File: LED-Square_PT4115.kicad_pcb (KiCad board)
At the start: 2 copper layers, 50 x 50 mm, 28 parts, among them P1 IN, P2 OUT, U1 PT4115-SOT89-5

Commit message: Fooling around a bit.
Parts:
- C1: footprint -C1206 -> my_parts:MADW__C0805
- C2, C3, C4, C5, C6: footprint -C0805 -> my_parts:MADW__C0805
- D1, D2, D3, D4, D5, D6: footprint MADW__Nichia-NSS-LED__handsolder -> my_parts:MADW__Nichia-NT2x757DT
- DS1: value MBRS140T3G -> SS14L (40V, 1A); footprint MADW__diode-SMB-package -> my_parts:MADW__diode_sub-SMA
- DZ1: footprint -SOT23 -> my_parts:MADW__SOT23
- R1, R2, R_CS1: footprint -R0805 -> my_parts:MADW__R0805
- moved DS1 1.60 mm to (82.8, 111.4)
- moved R2 1.05 mm to (92.9, 120.0)
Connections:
- P1 pad 5: (no net) -> Net-(P1-Pad5)
- P2 pad 2: (no net) -> Net-(P2-Pad2)
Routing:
- net GND: track 82.5 -> 192.2 mm, vias 8 -> 19
- net VCC: track 134.0 -> 137.6 mm
- net /SW: track 17.6 -> 14.8 mm
- net /D6HS: track 12.5 -> 11.4 mm
- net /D4HS: track 26.7 -> 27.8 mm
- net /D1HS: track 26.7 -> 27.8 mm
- net /CSN: track 30.9 -> 30.0 mm
- net /_dim: track 20.7 -> 21.3 mm
- removed copper zone on F.Cu, net (none)
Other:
- board text added: "2014 - blog.spitzenpfeil.org"
- board text added: "L1: 100µH RCS_1: 0R6 -> 0.167A D1...: Nichia NT2x757DT equiv."
- board text added: "LED Square V1.1.a"
- board text added: "U1: PT4115 DS1: SS14L DZ1: BZX84C_5V1 R2: 1k"
- board text removed: "2013 - blog.spitzenpfeil.org"
- board text removed: "L1: 100µH RCS_1: 1R -> 0.1A D1...: Nichia NSSL157AT-H3 equiv."
- board text removed: "LED Square V1.0"
- board text removed: "U1: PT4115 DS1: MBRS140T3G DZ1: BZX84C_5V1 R2: 1k"

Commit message: R_CS --> 1206. Couldn't get 1R1 in 0805.
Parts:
- added R_CS2: 1R1, my_parts:MADW__R1206, F.Cu at (77.0, 111.4)
- G1: value LOGO -> OSHW-logo_silkscreen_5mm; footprint (none) -> oshw-logo:OSHW-logo_silkscreen_5mm
- G2: value LOGO -> LED_smile_silkscreen_5mm; footprint LOGO -> led-smile:LED_smile_silkscreen_5mm
- G3: renamed from G6; value LOGO -> KiCad LOGO
- R_CS1: value 1R -> 1R1; footprint my_parts:MADW__R0805 -> my_parts:MADW__R1206
- moved G2 5.00 mm to (87.0, 132.0)
- moved R_CS1 1.01 mm to (74.0, 111.4)
- moved G1 0.26 mm to (87.0, 101.0)
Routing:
- net GND: track 192.2 -> 178.7 mm, vias 19 -> 17
- net VCC: track 137.6 -> 147.0 mm
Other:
- board text added: "L1: 100µH RCS_1: (1R1)/2 -> 0.180A D1...: Nichia NT2x757DT equiv."
- board text added: "LED Square V1.11.a"
- board text removed: "L1: 100µH RCS_1: 0R6 -> 0.167A D1...: Nichia NT2x757DT equiv."
- board text removed: "LED Square V1.1.a"

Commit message: Tweaks.
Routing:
- net GND: track 178.7 -> 173.3 mm

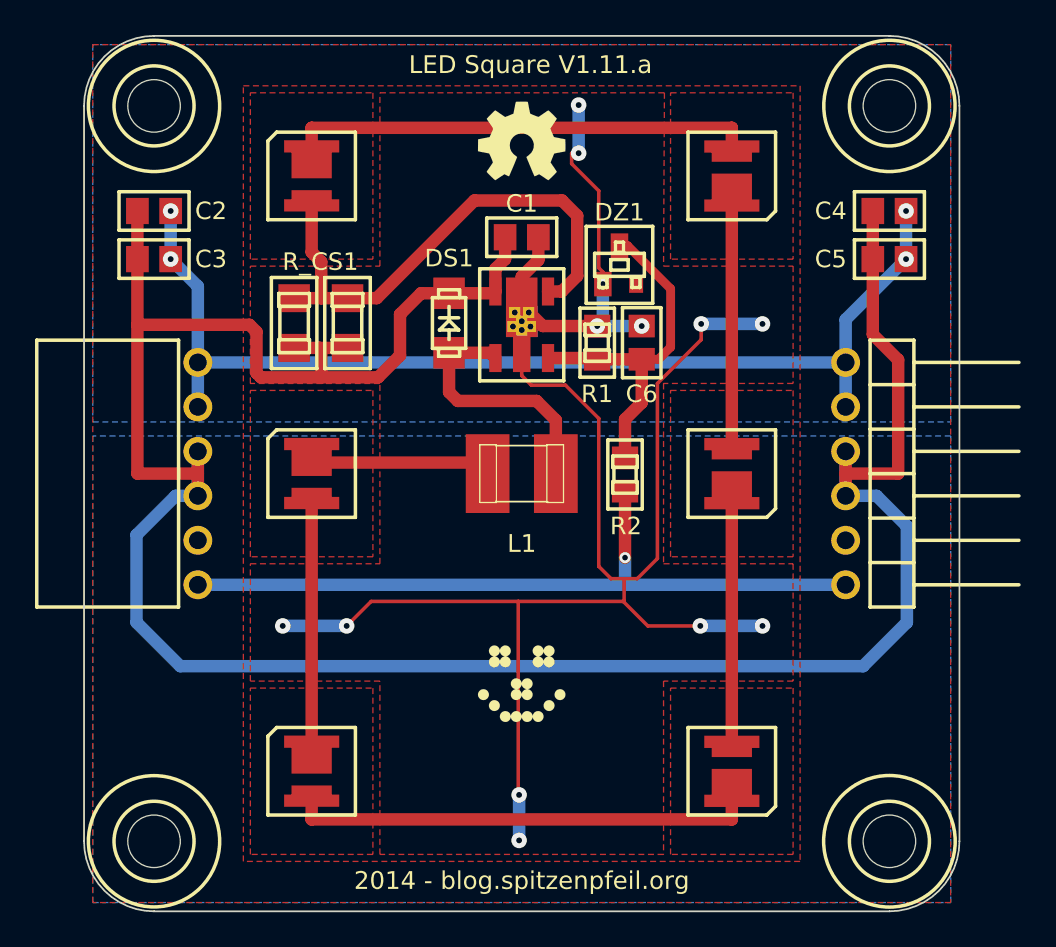
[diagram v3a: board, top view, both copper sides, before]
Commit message: Used B_Cu as heatsink again.
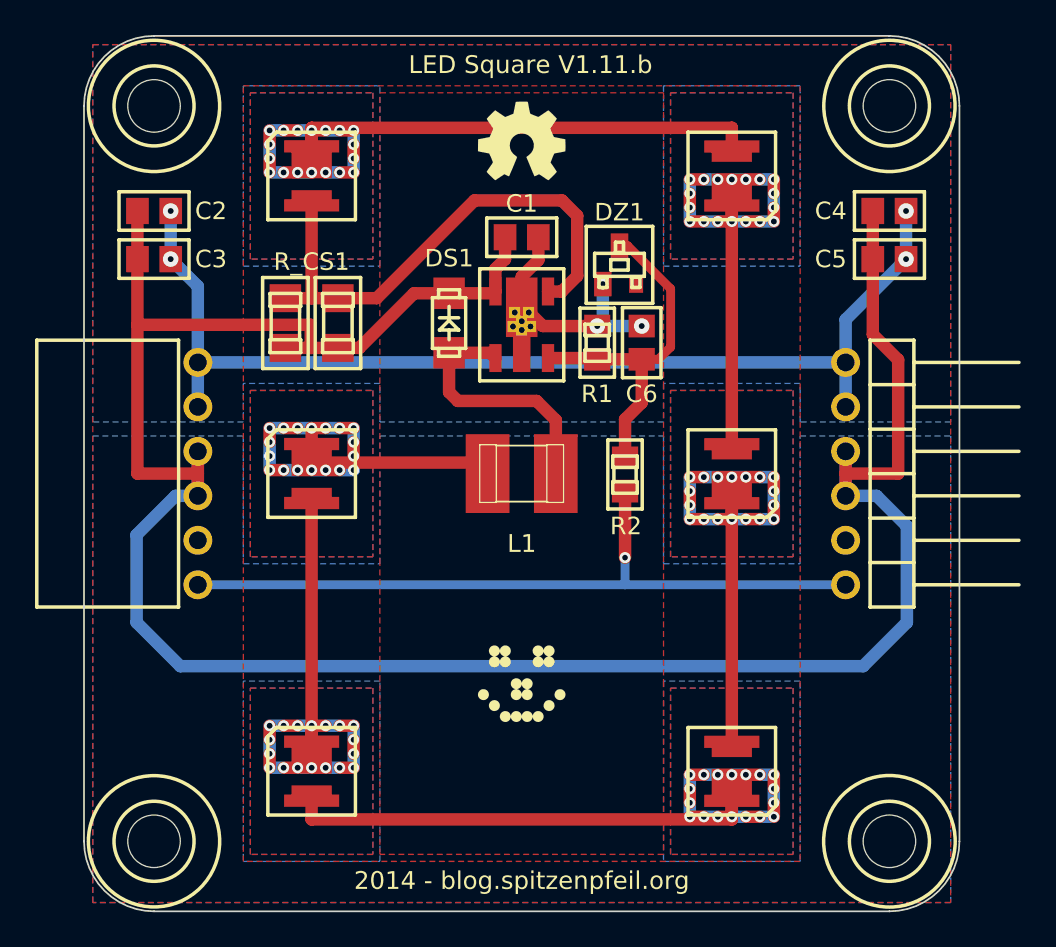
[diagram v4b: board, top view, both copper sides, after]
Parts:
- moved R_CS2 0.55 mm to (76.5, 111.4)
- moved R_CS1 0.50 mm to (73.5, 111.4)
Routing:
- net GND: track 173.3 -> 81.2 mm, vias 17 -> 7
- net /D1HS: track 27.8 -> 45.7 mm, vias 0 -> 18
- net /D2HS: track 15.3 -> 30.6 mm, vias 0 -> 18
- net /D3HS: track 15.3 -> 30.6 mm, vias 0 -> 18
- net /D5HS: track 15.3 -> 30.6 mm, vias 0 -> 18
- net /D4HS: track 27.8 -> 43.1 mm, vias 0 -> 18
- net /D6HS: track 11.4 -> 26.7 mm, vias 0 -> 18
- net VCC: track 147.0 -> 140.4 mm
- added copper zone on B.Cu, net /D1HS
- added copper zone on B.Cu, net /D2HS
- added copper zone on B.Cu, net /D3HS
- added copper zone on B.Cu, net /D4HS
- added copper zone on B.Cu, net /D5HS
- added copper zone on B.Cu, net /D6HS
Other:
- board text added: "L1: 100µH RCS_1: (1R0)/2 -> 0.2A D1...: Nichia NT2x757DT equiv."
- board text added: "LED Square V1.11.b"
- board text removed: "L1: 100µH RCS_1: (1R1)/2 -> 0.180A D1...: Nichia NT2x757DT equiv."
- board text removed: "LED Square V1.11.a"

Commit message: Heatsink tweaks.
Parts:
- moved R2 8.62 mm to (97.0, 112.5)
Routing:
- net /DIM: track 42.3 -> 51.7 mm
- net /_dim: track 21.1 -> 18.1 mm
- net /D4HS: track 43.1 -> 45.0 mm
- net /D1HS: track 45.7 -> 47.5 mm
- net /CSN: track 30.7 -> 29.6 mm
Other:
- board text added: "LED Square V1.11.c"
- board text removed: "LED Square V1.11.b"

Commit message: Silkscreen tweaks.
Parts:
- removed G3: KiCad LOGO, LOGO
- added G***: fire_silkscreen-back_4mm, fire:fire_silkscreen-back_4mm, B.Cu at (91.2, 120.0)
- added G***: fire_silkscreen-back_4mm, fire:fire_silkscreen-back_4mm, B.Cu at (82.8, 120.0)
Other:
- board text added: "C6: soft-start: 1.25µF/s (remove for ext. PWM) R1: 1M with soft-start, 10k with ext. PWM"
- board text added: "L1: 100µH RCS_1: 0.5R->0.2A D1...: Nichia NT2x757DT equiv."
- board text added: "VCC: 18-24V DC DIM: 5V PWM or 0-2.5V DC"
- board text removed: "L1: 100µH RCS_1: (1R0)/2 -> 0.2A D1...: Nichia NT2x757DT equiv."
- board text removed: "VCC: 18-24V DC DIM: 5V PWM or 0-2.5V DC C6: soft-start: 1.25µF/s (remove for ext. PWM) R1: 1M with soft-start, 10k with ext. PWM"
- board text removed: "http://www.flickr.com/groups/kicad"

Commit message: Copper pour tweaks.
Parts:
- moved R2 0.30 mm to (96.8, 112.5)
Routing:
- net VCC: track 140.4 -> 75.2 mm
- net /D5HS: track 30.6 -> 29.5 mm
- net /D3HS: track 30.6 -> 29.5 mm
- net /DIM: track 51.7 -> 50.9 mm
- net /_dim: track 18.1 -> 17.3 mm
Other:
- board text added: "LED Square V1.11.d"
- board text removed: "LED Square V1.11.c"

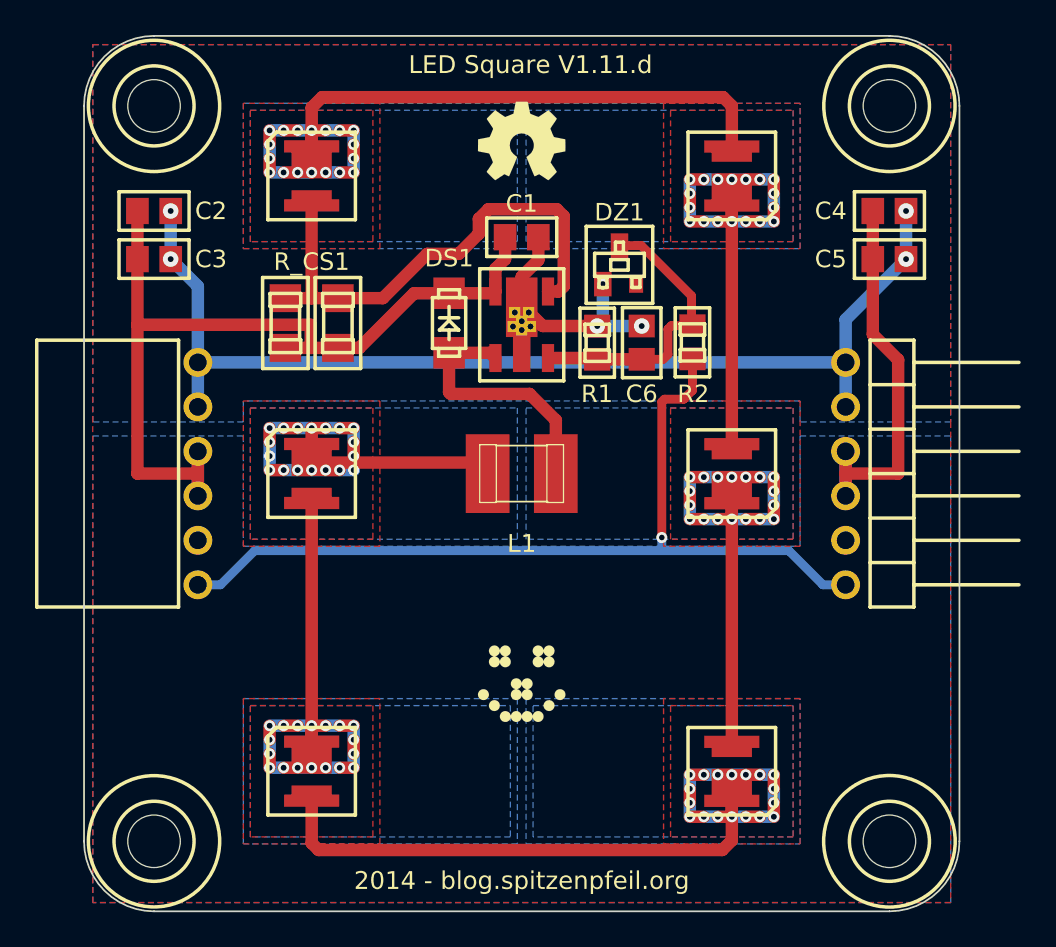
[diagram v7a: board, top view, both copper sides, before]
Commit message: More thermal vias for LEDs.
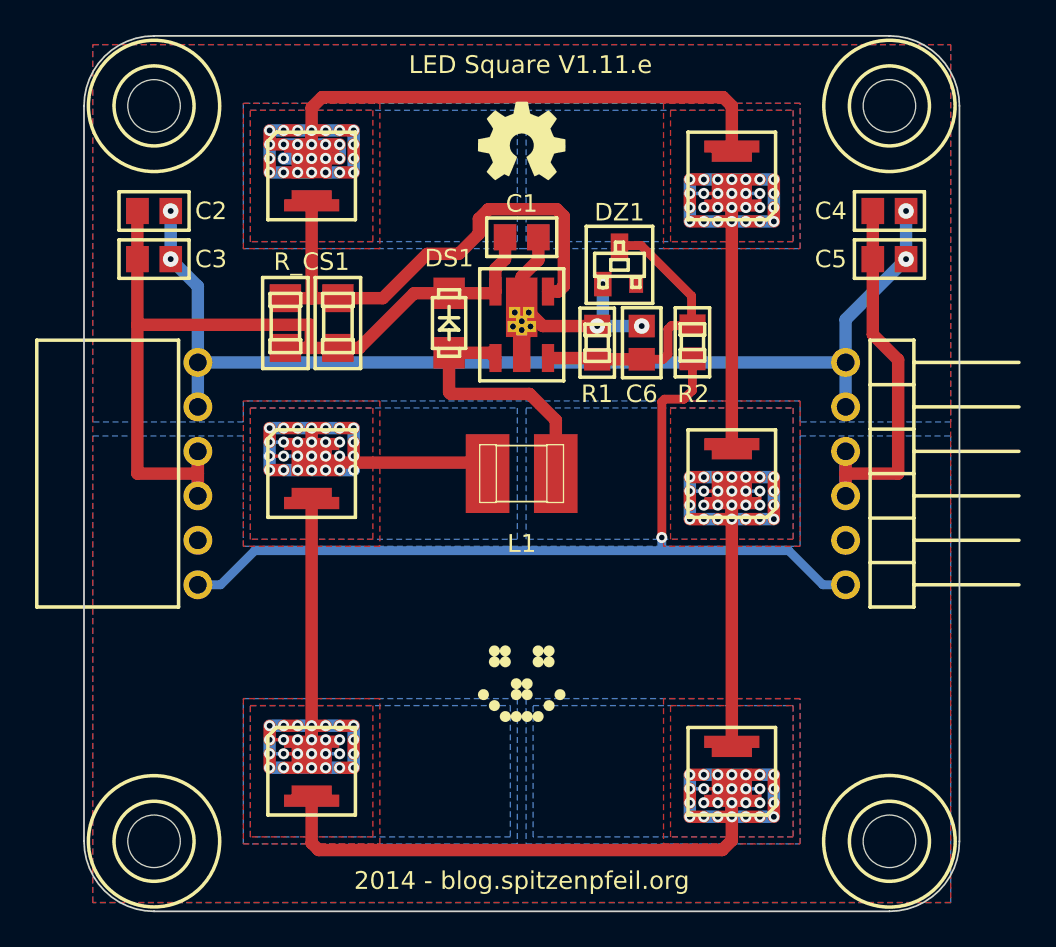
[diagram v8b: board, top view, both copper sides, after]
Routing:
- net /D6HS: track 26.7 -> 34.7 mm, vias 18 -> 28
- net /D5HS: track 29.5 -> 37.5 mm, vias 18 -> 28
- net /D4HS: track 45.0 -> 53.0 mm, vias 18 -> 28
- net /D3HS: track 29.5 -> 37.5 mm, vias 18 -> 28
- net /D2HS: track 30.6 -> 38.6 mm, vias 18 -> 28
- net /D1HS: track 47.5 -> 55.5 mm, vias 18 -> 28
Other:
- board text added: "LED Square V1.11.e"
- board text removed: "LED Square V1.11.d"
